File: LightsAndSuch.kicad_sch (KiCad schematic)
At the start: 4 parts, among them U1 STM32F205RBTx, U2 MAX98357A, U5 4068

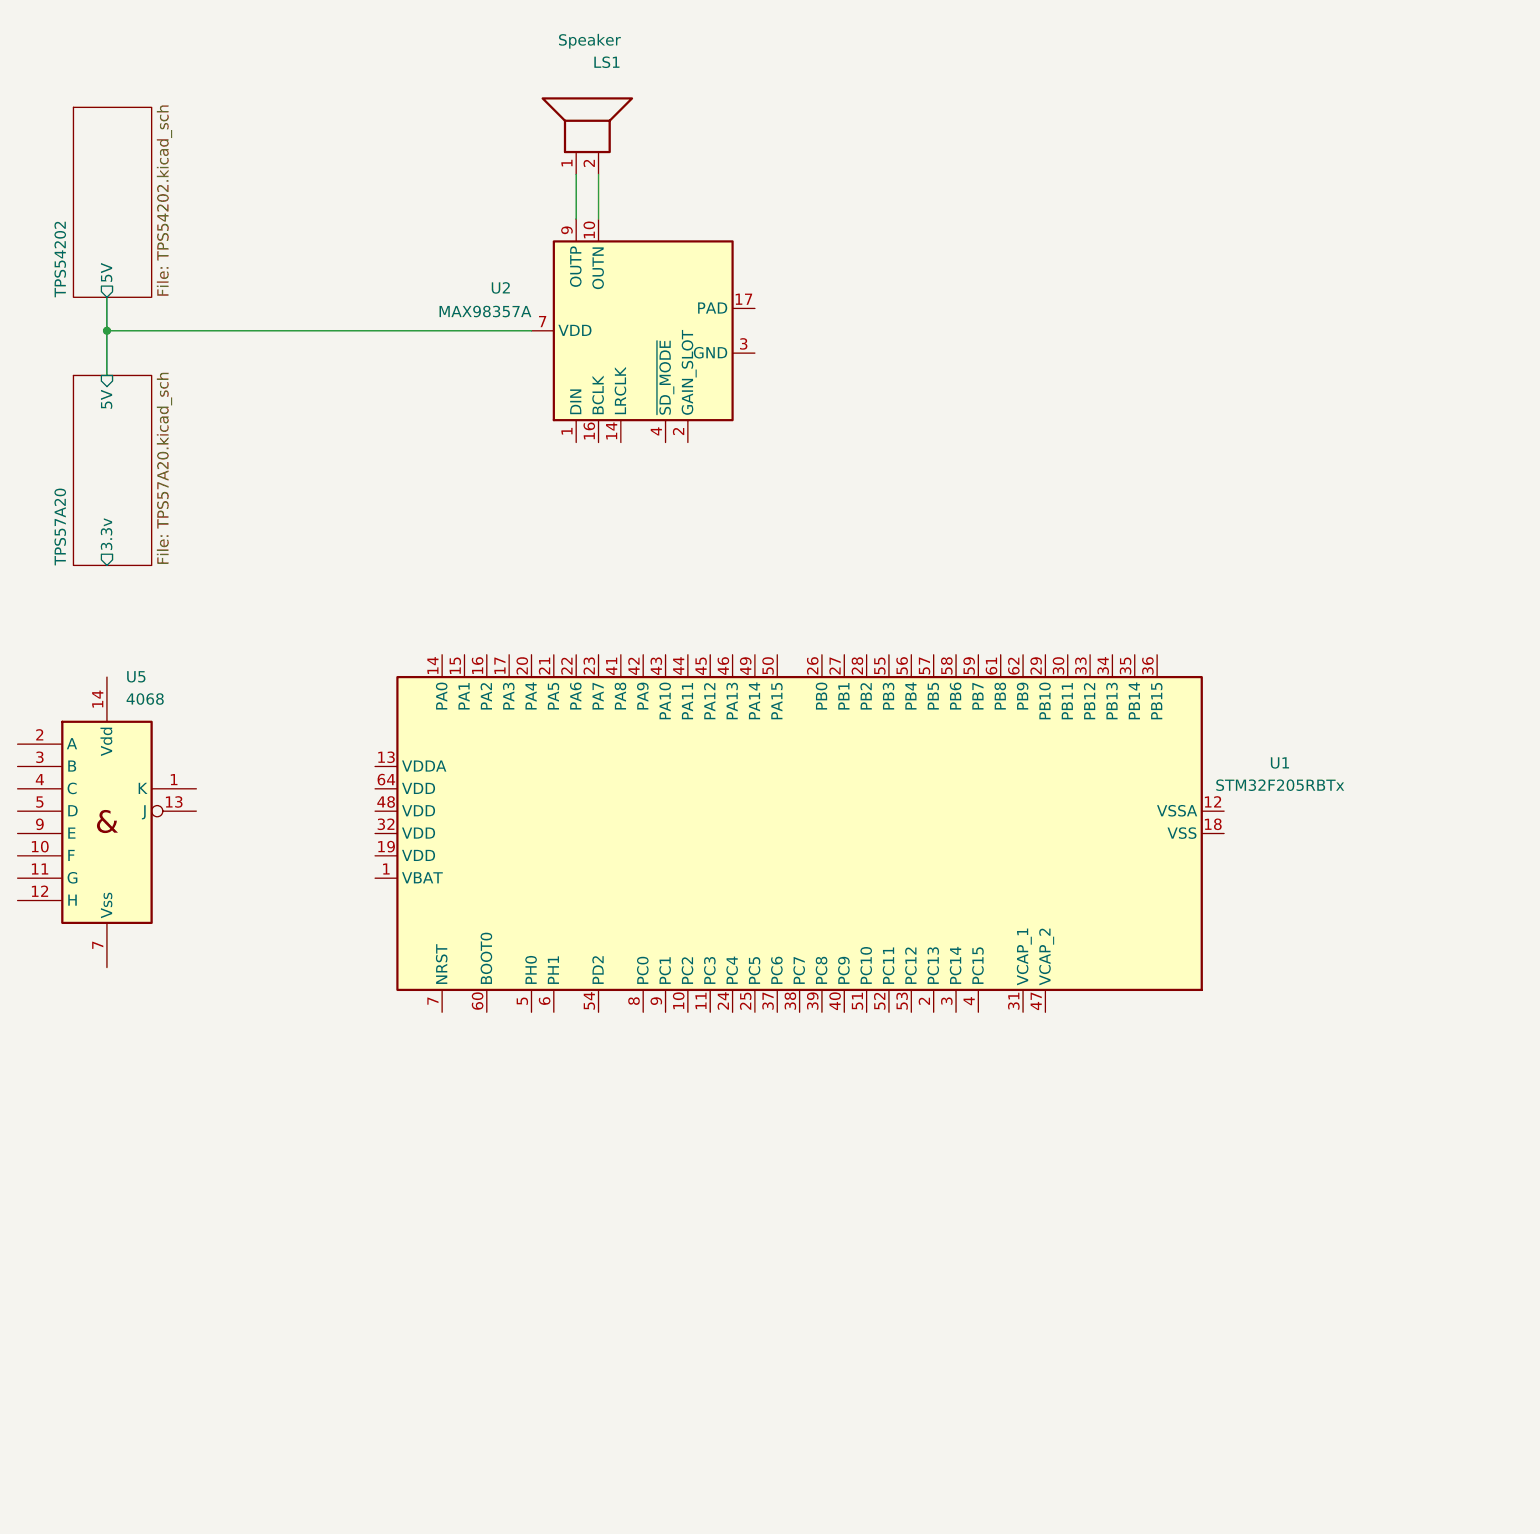
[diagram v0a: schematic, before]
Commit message: decoupling capacitors for uC and DAC
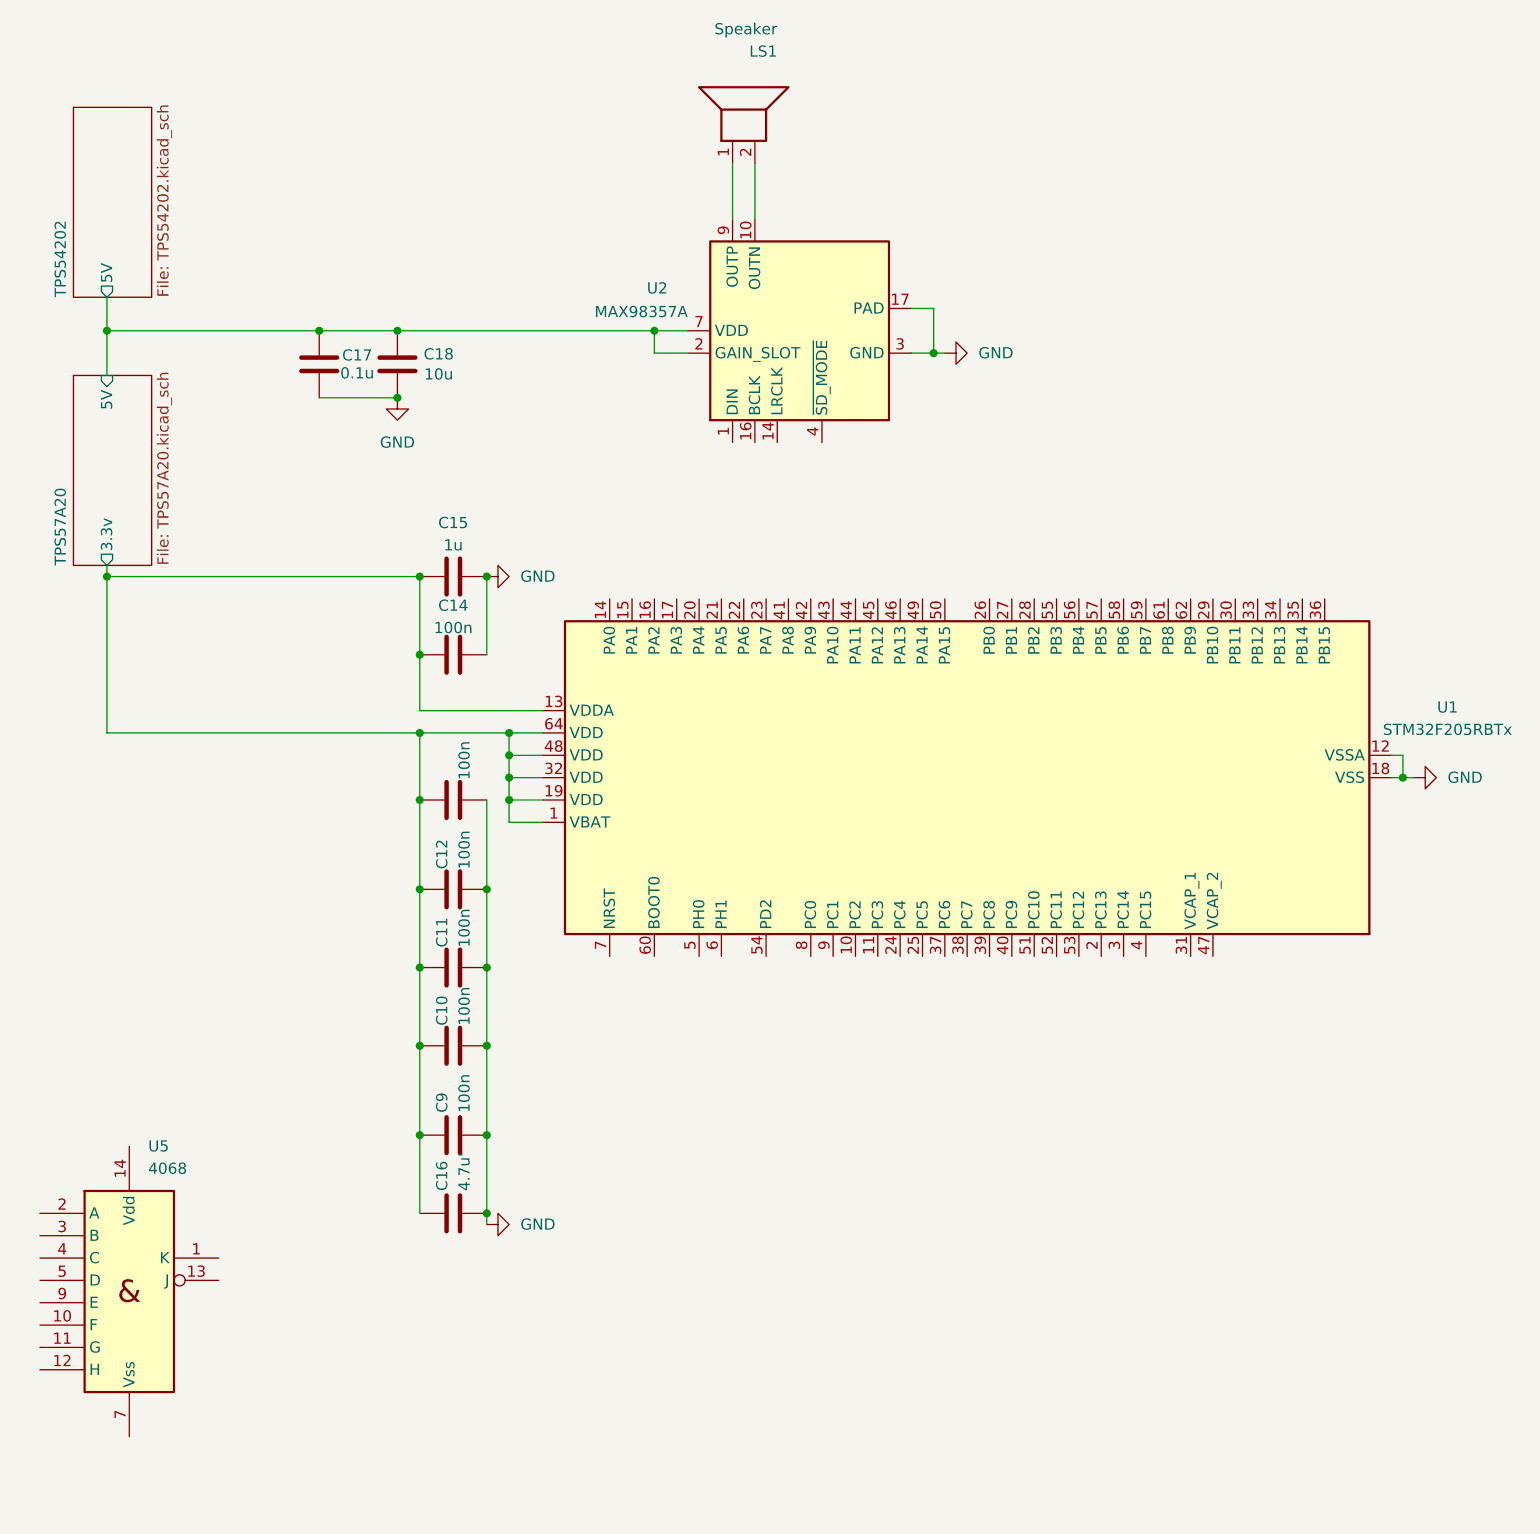
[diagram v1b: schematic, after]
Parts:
- added C10, C11, C12, C13, C14, C9: 100n, symbol Device:C
- added C15: 1u, symbol Device:C
- added C16: 4.7u', symbol Device:C
- added C17: 0.1u, symbol Device:C
- added C18: 10u, symbol Device:C
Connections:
- net TPS54202/5V: now also U2.2 (GAIN_SLOT), C17.2, C18.2
- net TPS57A20/3.3v: now also U1.1 (VBAT), U1.13 (VDDA), U1.19 (VDD), U1.32 (VDD), U1.48 (VDD), U1.64 (VDD), C10.1, C11.1, C12.1, C13.1, C14.2, C15.2, C16.1, C9.1
- net GND: now reaches U2.11 (GND), U2.15 (GND), U2.3 (GND)
- net GND: now also U1.12 (VSSA), U1.18 (VSS), U1.63 (VSS), U2.17 (PAD), C10.2, C11.2, C12.2, C13.2, C14.1, C15.1, C16.2, C17.1, C18.1, C9.2
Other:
- moved on the sheet: LS1, U2, U5

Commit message: changed AND gate, all connections should be finished
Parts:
- removed U5: 4068, symbol 4xxx_IEEE:4068
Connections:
- net TPS57A20/3.3v is gone; now on net 3.3V: C10.1, C11.1, C12.1, C13.1, C14.2, C15.2, C16.1, C9.1, U1.1 (VBAT), U1.13 (VDDA), U1.19 (VDD), U1.32 (VDD), U1.48 (VDD), U1.64 (VDD)
- net at U1.34 (PB13): now also U2.16 (BCLK)
- net at U1.36 (PB15): now also U2.1 (DIN)
- net at U1.62 (PB9): now also U2.14 (LRCLK)
- net CD4081B/Trigger: now reaches U1.8 (PC0)
- net 3.3V: now reaches U2.4 (~{SD_MODE})
- net TPS54202/5V renamed 5V
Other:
- added sheet CD4081B (CD4081B.kicad_sch)
- moved on the sheet: C10, C11, C12, C14, C15, C16, C17, C18, C9, LS1, U1, U2
